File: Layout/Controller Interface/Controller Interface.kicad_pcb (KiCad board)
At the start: 2 copper layers, 50 x 50 mm, 59 parts, among them J1 USB_C_Receptacle_USB2.0, J2 Controller 2, J3 Controller 3, J4 Controller 4, J6 Conn_01x02_Pin, J7 Controller 1, Q1 AO3401A, Q2 AO3401A, Q3 AO3401A, SW1 SW_Push, SW2 SW_Push, SW3 SW_Push, SW4 SW_Push, U1 RP2040, U3 W25X40CLSN, U4 MCP73812T-420I-OT, U5 TPS613222ADBZ, U7 MIC5504-3.3YM5, Y1 12MHz

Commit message: Completed schematic and layout
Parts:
- removed H3, H4: MountingHole_Pad, MountingHole:MountingHole_2.2mm_M2_DIN965
- removed SW2: SW_Push, Button_Switch_SMD:SW_SPST_TL3342
- removed U6: ~, RF_Module:nRF24L01_Mini
- removed Y1: 12MHz, Crystal:Crystal_SMD_3225-4Pin_3.2x2.5mm_HandSoldering
- removed locked: LED, LED_SMD:LED_0805_2012Metric
- added C11: 2u2, Capacitor_SMD:C_0603_1608Metric, B.Cu at (161.2, 97.0)
- added C12: 100n, Capacitor_SMD:C_0603_1608Metric, B.Cu at (161.2, 91.5)
- added C13: 100n, Capacitor_SMD:C_0603_1608Metric, B.Cu at (161.2, 89.9)
- added C14: 100n, Capacitor_SMD:C_0603_1608Metric, B.Cu at (161.2, 93.3)
- added C15: 2u2, Capacitor_SMD:C_0603_1608Metric, B.Cu at (154.8, 92.2)
- added C16: 100n, Capacitor_SMD:C_0603_1608Metric, B.Cu at (156.8, 98.4)
- added C17: 100n, Capacitor_SMD:C_0603_1608Metric, B.Cu at (161.2, 95.0)
- added C18: 100n, Capacitor_SMD:C_0603_1608Metric, B.Cu at (161.2, 98.7)
- added C19: 100n, Capacitor_SMD:C_0603_1608Metric, B.Cu at (150.5, 91.3)
- added C20: 100n, Capacitor_SMD:C_0603_1608Metric, B.Cu at (157.8, 92.2)
- added D1: LED, LED_SMD:LED_0805_2012Metric, F.Cu at (143.3, 72.4)
- added D7: LED, LED_SMD:LED_0805_2012Metric, F.Cu at (132.8, 82.4)
- added D8: LED, LED_SMD:LED_0805_2012Metric, F.Cu at (132.8, 92.9)
- added D9: LED, LED_SMD:LED_0805_2012Metric, F.Cu at (132.8, 96.9)
- added R13: 1K, Resistor_SMD:R_0603_1608Metric, B.Cu at (149.3, 88.2)
- added R14: 100, Resistor_SMD:R_0805_2012Metric, F.Cu at (132.8, 86.0)
- added U2: RP2040, Package_DFN_QFN:QFN-56-1EP_7x7mm_P0.4mm_EP3.2x3.2mm, F.Cu at (155.8, 94.9)
- added Y2: Crystal_GND24, Crystal:Crystal_SMD_Abracon_ABM8G-4Pin_3.2x2.5mm, B.Cu at (155.8, 94.9)
- C1: value 15p -> 100n; footprint Capacitor_SMD:C_0805_2012Metric -> Capacitor_SMD:C_0603_1608Metric
- C2: value 15p -> 2u2; footprint Capacitor_SMD:C_0805_2012Metric -> Capacitor_SMD:C_0603_1608Metric
- C3: value 2u2 -> 15p; footprint Capacitor_SMD:C_0805_2012Metric -> Capacitor_SMD:C_0603_1608Metric
- C4: value 100n -> 15p; footprint Capacitor_SMD:C_0805_2012Metric -> Capacitor_SMD:C_0603_1608Metric
- J1: footprint Connector_USB:USB_C_Receptacle_HRO_TYPE-C-31-M-12 -> Connector_USB:USB_C_Receptacle_GCT_USB4105-xx-A_16P_TopMnt_Horizontal
- R19, R20: value 5.1K -> 100; moved to F.Cu
- R6, R7: value 1K -> 27; footprint Resistor_SMD:R_0805_2012Metric -> Resistor_SMD:R_0603_1608Metric; moved to F.Cu
- R8, R9: value 27 -> 5K1; footprint Resistor_SMD:R_0805_2012Metric -> Resistor_SMD:R_0603_1608Metric
- SW1: value SW_Push -> PWR
- SW3: value SW_Push -> SW_PAIR; moved to F.Cu
- SW4: value SW_Push -> SW_BOOT; moved to B.Cu
- U1: value RP2040 -> W25Q32JVSS; footprint Package_DFN_QFN:QFN-56-1EP_7x7mm_P0.4mm_EP3.2x3.2mm -> Package_SO:SOIC-8_5.23x5.23mm_P1.27mm
- U3: value W25X40CLSN -> ~; footprint Package_SO:SOIC-8_3.9x4.9mm_P1.27mm -> GTS24:GTS24-SMD
- moved R6 109.4 mm to (156.2, 81.1), turned to 0 degrees
- moved R7 108.4 mm to (155.7, 83.0), turned to 0 degrees
- moved H2 92.3 mm to (134.8, 115.9)
- moved R20 91.8 mm to (134.9, 96.9), turned to 90 degrees
- moved R19 91.2 mm to (134.9, 92.9), turned to 90 degrees
- moved U3 53.9 mm to (155.8, 111.0), turned to 0 degrees
- moved SW3 49.8 mm to (143.3, 94.9), turned to 0 degrees
- moved SW4 46.5 mm to (136.1, 87.2)
- moved C4 46.3 mm to (158.8, 95.0), turned to -90 degrees
- moved C5 43.5 mm to (168.8, 99.2), turned to 180 degrees
- moved C3 42.9 mm to (152.8, 94.8), turned to -90 degrees
- moved SW1 40.9 mm to (168.3, 94.9)
- moved C10 39.9 mm to (172.4, 99.2), turned to 0 degrees
- moved C9 39.7 mm to (178.2, 93.6), turned to -90 degrees
- moved R16 39.3 mm to (163.8, 72.5), turned to 0 degrees
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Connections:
- C1 pad 1: /Processor/XIN -> +3.3V
- C2 pad 1: /Processor/XOUT -> +3.3V
- C3 pad 1: +3.3V -> Net-(U2-XIN)
- C4 pad 1: +3.3V -> GND
- C4 pad 2: GND -> Net-(U2-XOUT)
- J1 pad A6: /Processor/USB_DP -> Net-(J1-D+-PadA6)
- J1 pad A7: /Processor/USB_DM -> Net-(J1-D--PadA7)
- J1 pad B6: /Processor/USB_DP -> Net-(J1-D+-PadA6)
- J1 pad B7: /Processor/USB_DM -> Net-(J1-D--PadA7)
- J2 pad 3: Net-(J2-Pad3) -> GND
- J2 pad 4: Net-(J2-Pad3) -> GND
- J3 pad 3: Net-(J3-Pad3) -> GND
- J3 pad 4: Net-(J3-Pad3) -> GND
- J4 pad 3: Net-(J4-Pad3) -> GND
- J4 pad 4: Net-(J4-Pad3) -> GND
- J7 pad 3: Net-(J7-Pad3) -> GND
- J7 pad 4: Net-(J7-Pad3) -> GND
- Q2 pad 3: Net-(Q1-S) -> Net-(D2-A)
- R19 pad 1: Net-(J1-CC2) -> TX_LED
- R19 pad 2: GND -> Net-(D8-A)
- R20 pad 1: Net-(J1-CC1) -> RX_LED
- R20 pad 2: GND -> Net-(D9-A)
- R6 pad 1: /Processor/XIN -> Net-(J1-D--PadA7)
- R6 pad 2: /Processor/XOUT -> /Processor/USB_DM
- R7 pad 1: /Processor/QSPI_SS -> Net-(J1-D+-PadA6)
- R7 pad 2: Net-(R7-Pad2) -> /Processor/USB_DP
- R8 pad 1: /Processor/USB_DP -> Net-(J1-CC1)
- R8 pad 2: Net-(U1-USB_DP) -> GND
- R9 pad 1: /Processor/USB_DM -> Net-(J1-CC2)
- R9 pad 2: Net-(U1-USB_DM) -> GND
- SW3 pad 1: /Processor/RUN -> /Processor/PAIR
- SW4 pad 1: /Processor/PAIR -> Net-(R13-Pad2)
- U1 pad 1: Net-(U1-IOVDD-Pad1) -> /Processor/QSPI_SS
- U1 pad 2: DATA_1 -> /Processor/QSPI_SD1
- U1 pad 3: DATA_2 -> /Processor/QSPI_SD2
- U1 pad 4: DATA_3 -> GND
- U1 pad 5: DATA_4 -> /Processor/QSPI_SD0
- U1 pad 6: CONT_1 -> /Processor/QSPI_SCLK
- U1 pad 7: CONT_2 -> /Processor/QSPI_SD3
- U1 pad 8: CONT_3 -> +3.3V
- U3 pad 1: /Processor/QSPI_SS -> +3.3V
- U3 pad 2: /Processor/QSPI_SD1 -> NRF_CE
- U3 pad 3: /Processor/QSPI_SD2 -> NRF_CS
- U3 pad 4: GND -> SPI0_CLK
- U3 pad 5: /Processor/QSPI_SD0 -> SPI0_MOSI
- U3 pad 6: /Processor/QSPI_SCLK -> SPI0_MISO
- U3 pad 7: /Processor/QSPI_SD3 -> NRF_IRQ
- U3 pad 8: +3.3V -> GND
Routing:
- net +3.3V: track 0.00 -> 151.0 mm, vias 0 -> 7
- net +5V: track 0.00 -> 114.8 mm
- net VBUS: track 0.00 -> 49.3 mm, vias 0 -> 1
- net +BATT: track 0.00 -> 33.5 mm
- net GND: track 0.00 -> 27.4 mm, vias 0 -> 1
- net PWR_ON: track 0.00 -> 26.4 mm, vias 0 -> 1
- net CONT_1: track 0.00 -> 22.7 mm
- net /Processor/PWR_LED: track 0.00 -> 22.7 mm
- net CONT_2: track 0.00 -> 22.5 mm
- net CONT_4: track 0.00 -> 22.3 mm
- net CONT_3: track 0.00 -> 22.1 mm
- net PWR_SW: track 0.00 -> 21.8 mm, vias 0 -> 1
- net RX_LED: track 0.00 -> 18.7 mm
- net DATA_2: track 0.00 -> 17.7 mm
- net DATA_1: track 0.00 -> 17.7 mm
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- removed copper zone on B.Cu, net (none)
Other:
- outline, holes or cut-outs redrawn

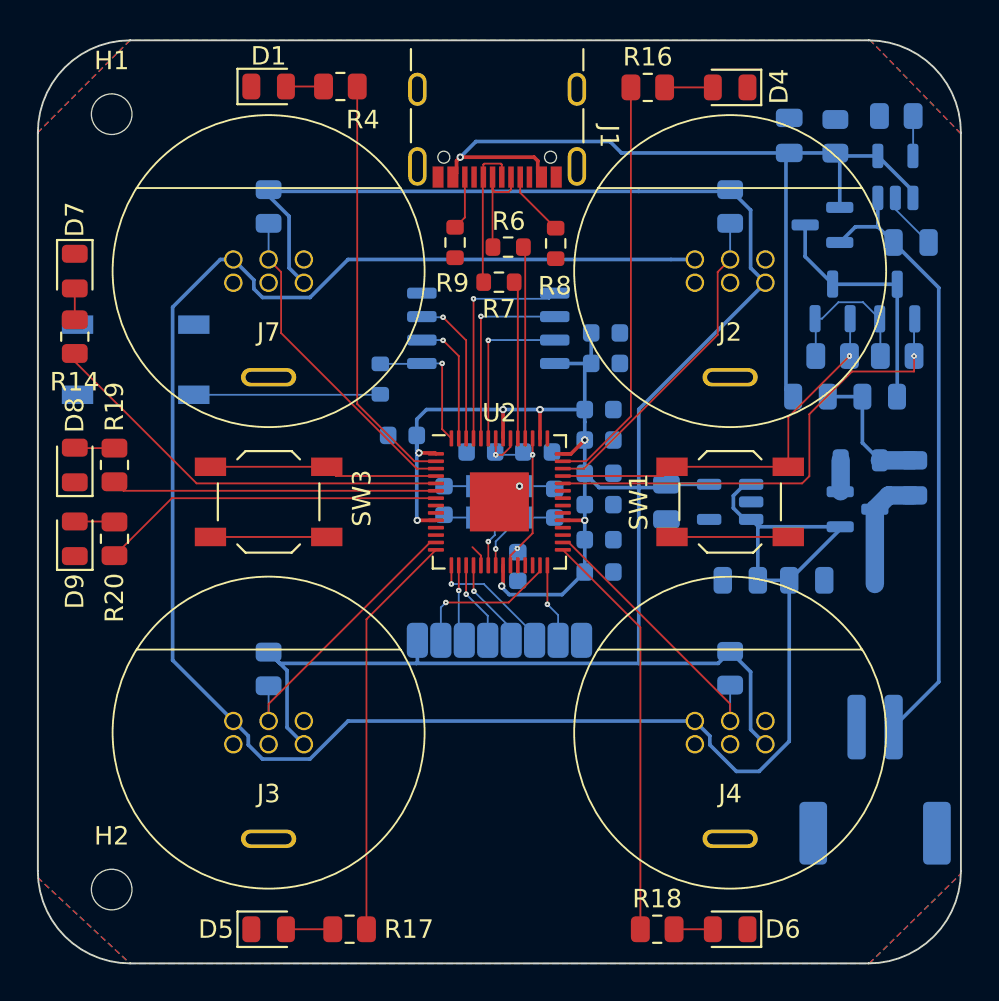
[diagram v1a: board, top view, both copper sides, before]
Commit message: Via too small
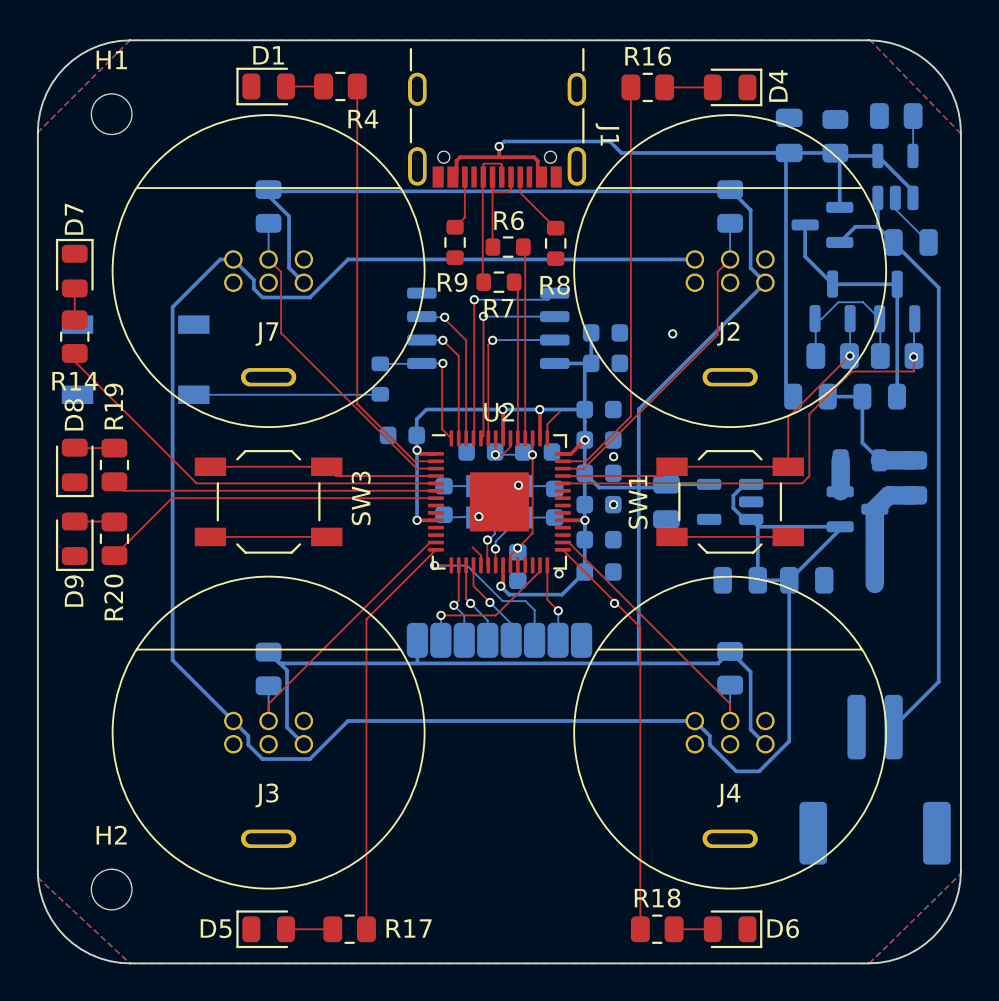
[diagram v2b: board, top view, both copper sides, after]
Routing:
- net SPI0_MISO: track 6.96 -> 8.97 mm
- net GND: track 27.4 -> 29.3 mm, vias 1 -> 6
- net VBUS: track 49.3 -> 47.5 mm
- net +3.3V: track 151.0 -> 150.5 mm
- net CONT_4: vias 0 -> 1

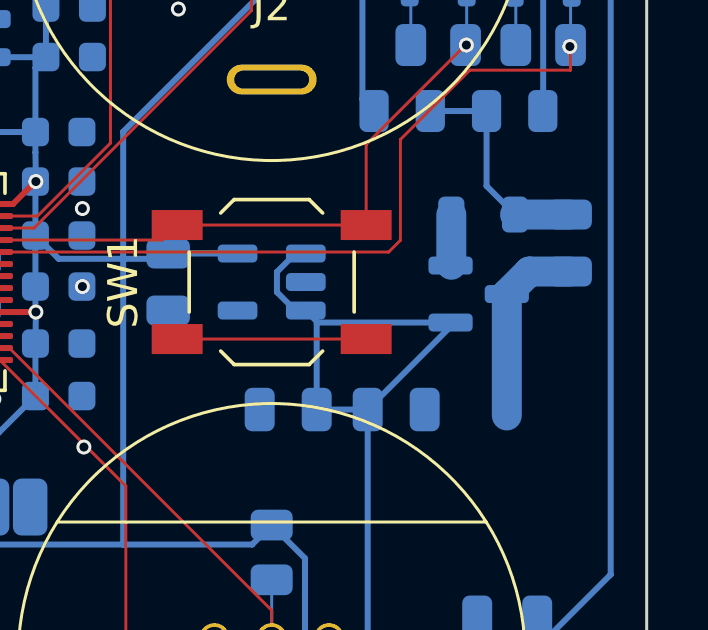
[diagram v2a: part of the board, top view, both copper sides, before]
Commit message: Switching regulator footprint doesn't exist
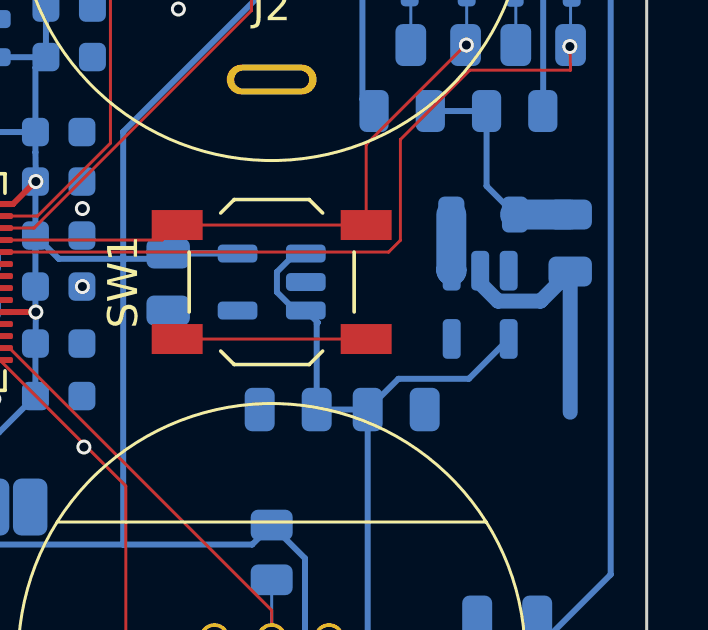
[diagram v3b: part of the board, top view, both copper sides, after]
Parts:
- C5, C6: value C -> 1u
- U5: value TPS613222ADBZ -> TPS613223ADBV; footprint Package_TO_SOT_SMD:SOT-23 -> Package_TO_SOT_SMD:SOT-23-5
- moved U5 0.36 mm to (175.2, 95.7), turned to -90 degrees
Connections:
- U5 pad 1: +5V -> Net-(U5-SW)
- U5 pad 2: Net-(U5-SW) -> GND
- U5 pad 3: GND -> unconnected-(U5-NC-Pad3)
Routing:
- net +5V: track 114.8 -> 112.0 mm
- net GND: track 29.3 -> 31.6 mm

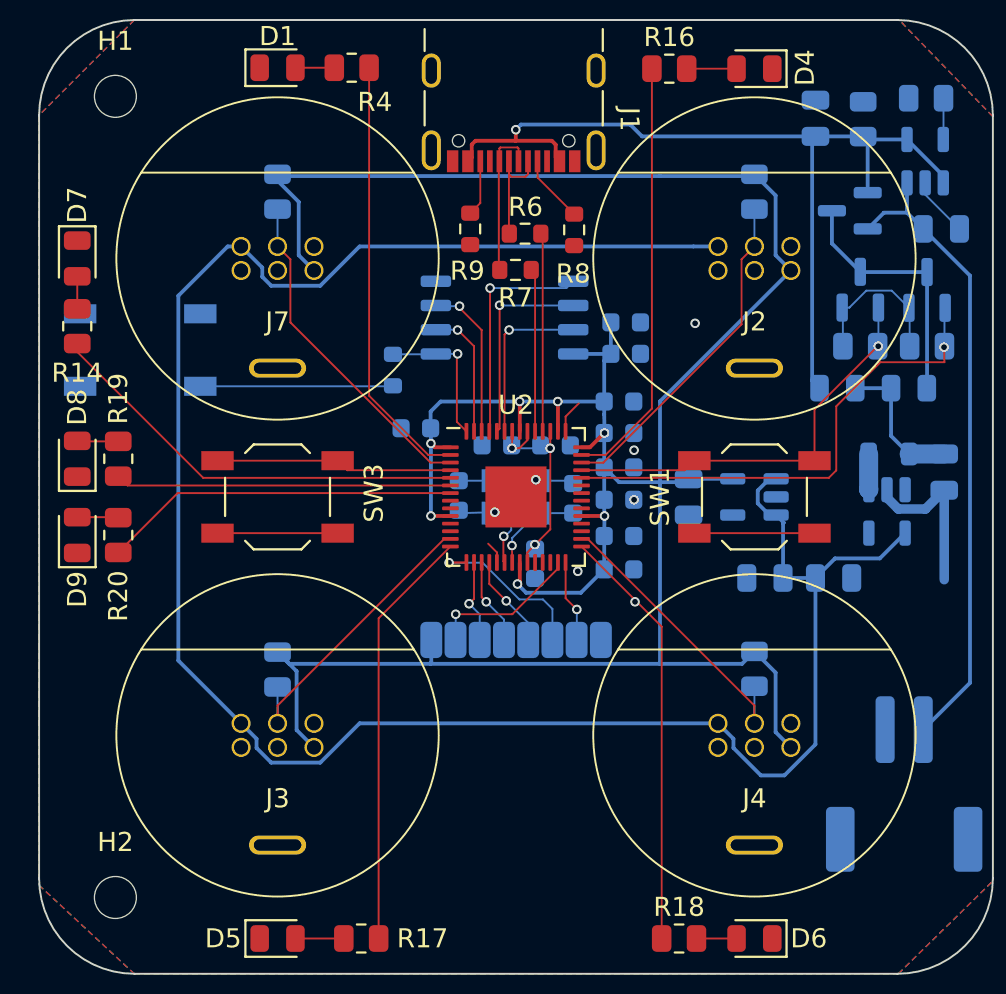
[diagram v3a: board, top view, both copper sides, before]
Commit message: Schematic/PCB fixes
Fix VUSB supply. Add cut out for antenna wire.
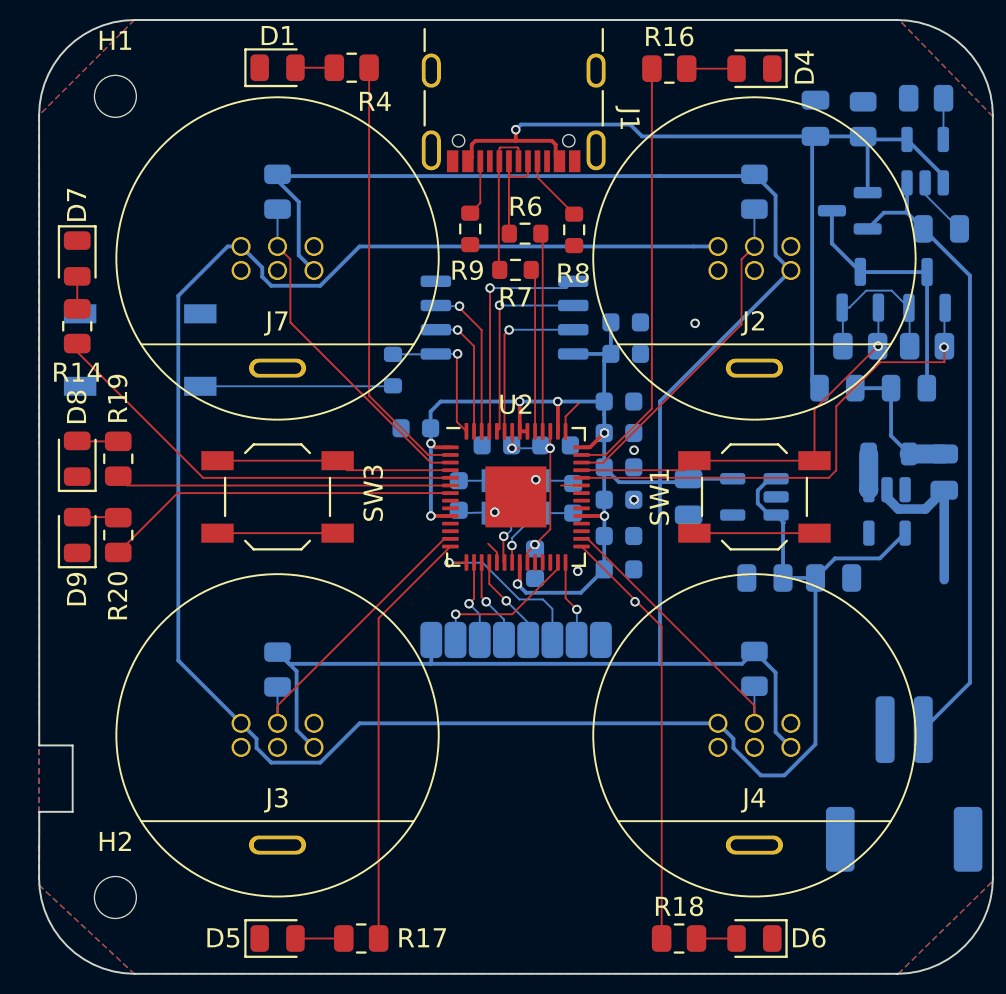
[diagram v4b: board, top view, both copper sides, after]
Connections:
- U2 pad 37: unconnected-(U2-GPIO25-Pad37) -> GND
- U2 pad 48: +1V1 -> +3.3V
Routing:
- net GND: track 31.6 -> 32.6 mm
- net +1V1: track 11.8 -> 10.7 mm
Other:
- outline, holes or cut-outs redrawn
